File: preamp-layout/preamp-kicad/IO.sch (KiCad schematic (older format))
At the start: 14 parts, among them J36 Conn_Coaxial_x2, J37 Conn_Coaxial_x2, J38 Conn_Coaxial_x2, J39 Conn_Coaxial_x2, J40 Conn_Coaxial_x2, J41 Conn_01x03_Female, J42 Conn_01x03_Female, J43 Conn_01x03_Female, J44 Conn_01x03_Female, J45 Conn_01x03_Female, J46 Conn_01x03_Male, J47 Conn_01x03_Male, J48 Conn_Coaxial_x2, J49 Conn_Coaxial_x2

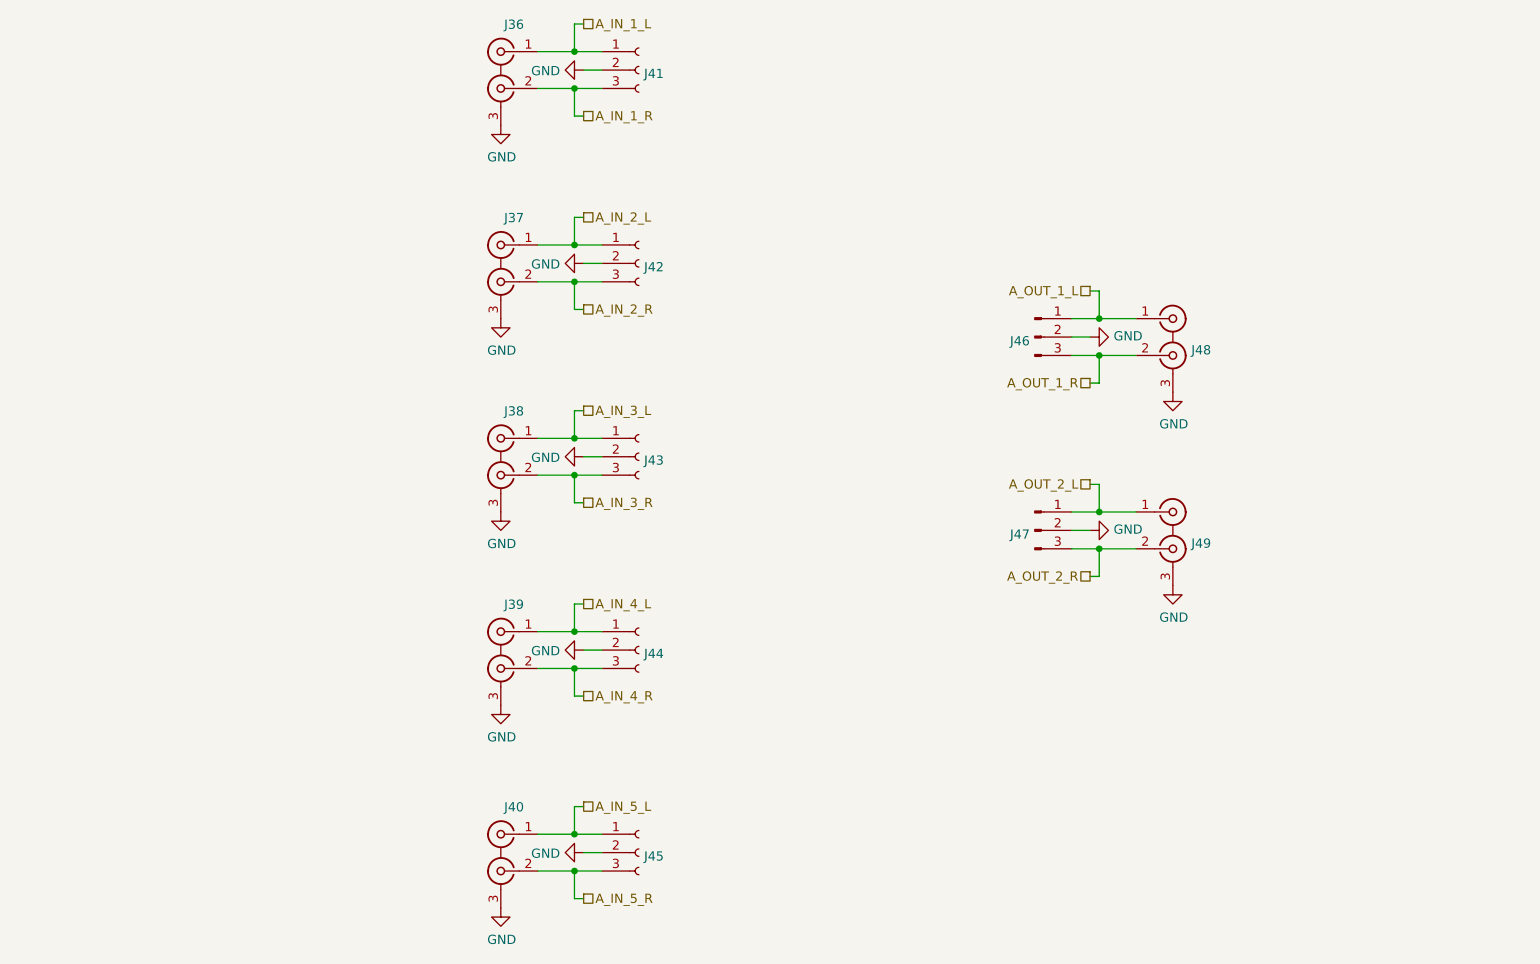
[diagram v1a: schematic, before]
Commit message: Power Supply Update
Grounding made more clear, tied to chassis on AC board. Pins renamed. Aligned with AC wall power convention. General cleanup.
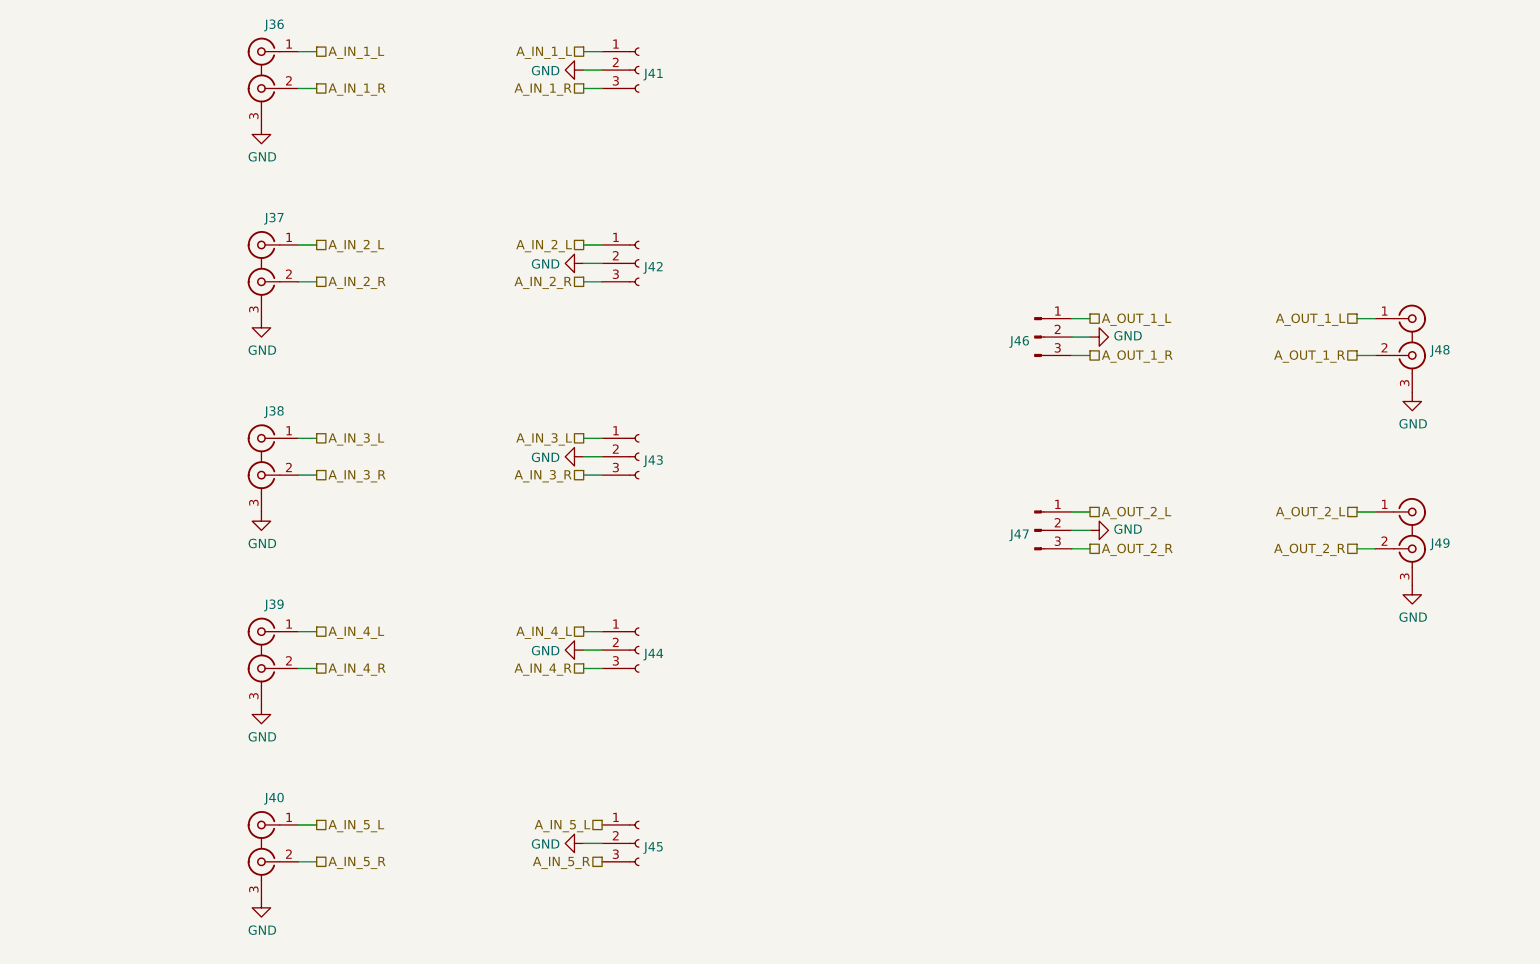
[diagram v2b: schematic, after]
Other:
- moved on the sheet: J36, J37, J38, J39, J40, J45, J48, J49

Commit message: Schematic layout updates
schematic optimization. Also implemented encoders with surrounding circuitry (self-contained on encoder board)
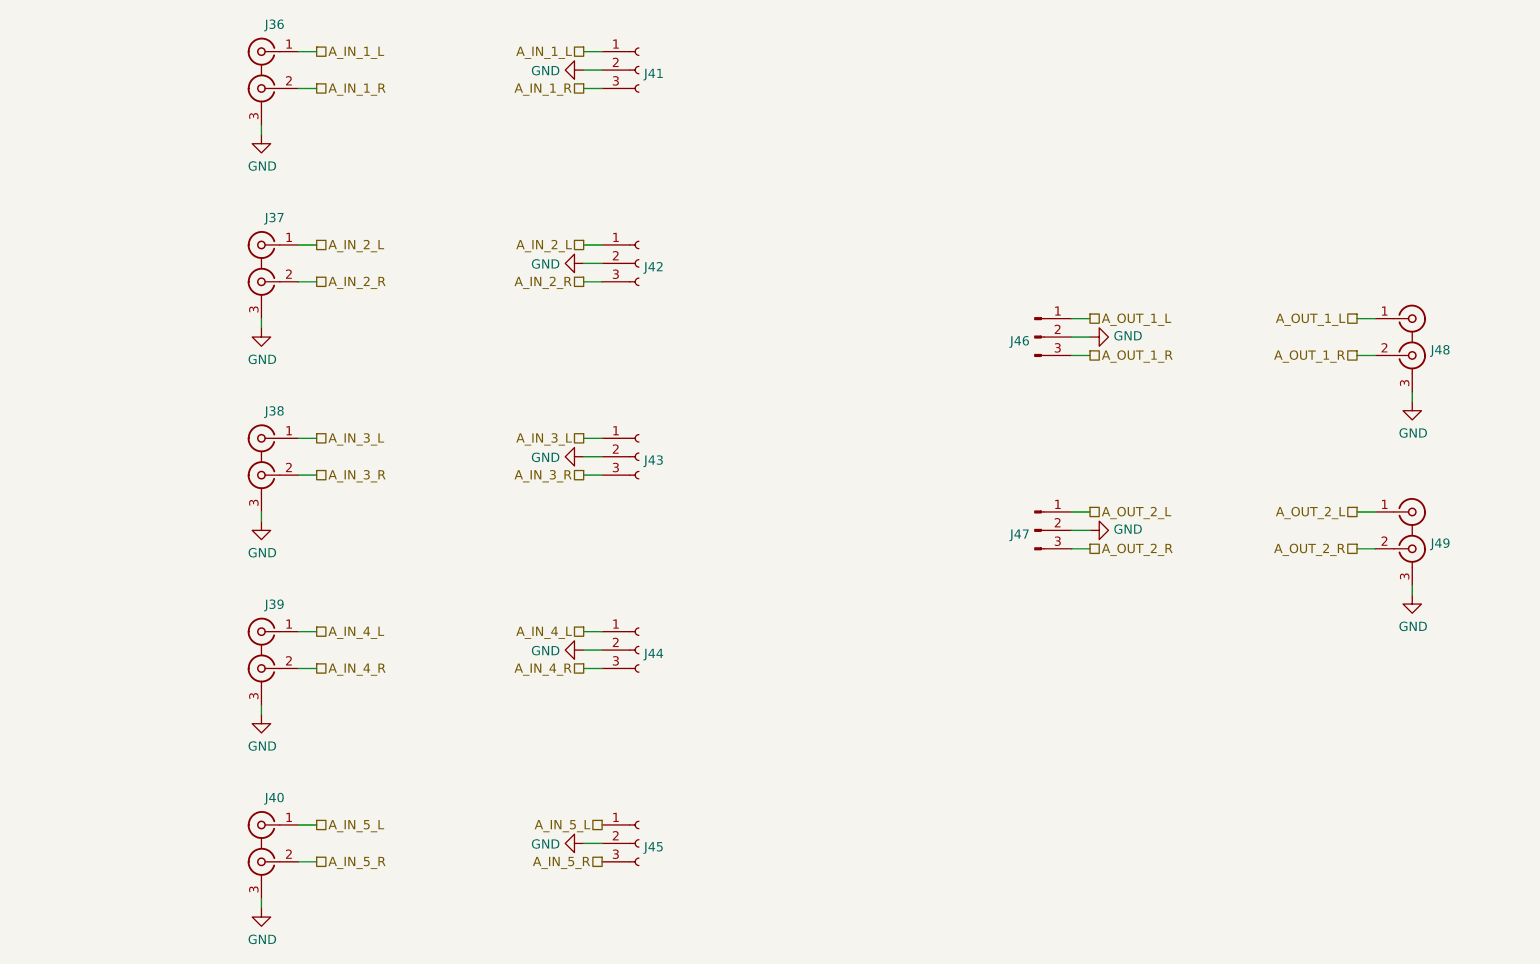
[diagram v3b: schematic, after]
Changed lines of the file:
@@
-$Comp
-L power:GND #PWR?
-U 1 1 64BAD508
-P 2800 6300
-AR Path="/5E26F6FE/64BAD508" Ref="#PWR?"  Part="1"
-AR Path="/5E607732/64BAD508" Ref="#PWR039"  Part="1"
-F 0 "#PWR039" H 2800 6050 50  0001 C CNN
-F 1 "GND" H 2805 6127 50  0000 C CNN
-F 2 "" H 2800 6300 50  0001 C CNN
-F 3 "" H 2800 6300 50  0001 C CNN
-	1    2800 6300
-	1    0    0    -1
-$EndComp
-$Comp
-L power:GND #PWR?
-U 1 1 64BAEC2E
-P 2800 5250
-AR Path="/5E26F6FE/64BAEC2E" Ref="#PWR?"  Part="1"
-AR Path="/5E607732/64BAEC2E" Ref="#PWR038"  Part="1"
-F 0 "#PWR038" H 2800 5000 50  0001 C CNN
-F 1 "GND" H 2805 5077 50  0000 C CNN
-F 2 "" H 2800 5250 50  0001 C CNN
-F 3 "" H 2800 5250 50  0001 C CNN
-	1    2800 5250
-	1    0    0    -1
-$EndComp
-$Comp
-L power:GND #PWR?
-U 1 1 64BB01CD
-P 2800 4200
-AR Path="/5E26F6FE/64BB01CD" Ref="#PWR?"  Part="1"
-AR Path="/5E607732/64BB01CD" Ref="#PWR037"  Part="1"
-F 0 "#PWR037" H 2800 3950 50  0001 C CNN
-F 1 "GND" H 2805 4027 50  0000 C CNN
-F 2 "" H 2800 4200 50  0001 C CNN
-F 3 "" H 2800 4200 50  0001 C CNN
-	1    2800 4200
-	1    0    0    -1
-$EndComp
-$Comp
-L power:GND #PWR?
-U 1 1 64BB1739
-P 2800 3150
-AR Path="/5E26F6FE/64BB1739" Ref="#PWR?"  Part="1"
-AR Path="/5E607732/64BB1739" Ref="#PWR036"  Part="1"
-F 0 "#PWR036" H 2800 2900 50  0001 C CNN
-F 1 "GND" H 2805 2977 50  0000 C CNN
-F 2 "" H 2800 3150 50  0001 C CNN
-F 3 "" H 2800 3150 50  0001 C CNN
-	1    2800 3150
-	1    0    0    -1
-$EndComp
 $Comp
 L power:GND #PWR?
 U 1 1 64BB2C61
-P 2800 2100
+P 2800 2150
 AR Path="/5E26F6FE/64BB2C61" Ref="#PWR?"  Part="1"
 AR Path="/5E607732/64BB2C61" Ref="#PWR035"  Part="1"
-F 0 "#PWR035" H 2800 1850 50  0001 C CNN
-F 1 "GND" H 2805 1927 50  0000 C CNN
-F 2 "" H 2800 2100 50  0001 C CNN
-F 3 "" H 2800 2100 50  0001 C CNN
-	1    2800 2100
-	1    0    0    -1
-$EndComp
-$Comp
-L power:GND #PWR?
-U 1 1 64BB4167
-P 9050 3550
-AR Path="/5E26F6FE/64BB4167" Ref="#PWR?"  Part="1"
-AR Path="/5E607732/64BB4167" Ref="#PWR047"  Part="1"
-F 0 "#PWR047" H 9050 3300 50  0001 C CNN
-F 1 "GND" H 9055 3377 50  0000 C CNN
-F 2 "" H 9050 3550 50  0001 C CNN
-F 3 "" H 9050 3550 50  0001 C CNN
-	1    9050 3550
-	1    0    0    -1
-$EndComp
-$Comp
-L power:GND #PWR?
-U 1 1 5EC97C75
-P 9050 4600
-AR Path="/5E26F6FE/5EC97C75" Ref="#PWR?"  Part="1"
-AR Path="/5E607732/5EC97C75" Ref="#PWR048"  Part="1"
-F 0 "#PWR048" H 9050 4350 50  0001 C CNN
-F 1 "GND" H 9055 4427 50  0000 C CNN
-F 2 "" H 9050 4600 50  0001 C CNN
-F 3 "" H 9050 4600 50  0001 C CNN
-	1    9050 4600
+F 0 "#PWR035" H 2800 1900 50  0001 C CNN
+F 1 "GND" H 2805 1977 50  0000 C CNN
+F 2 "" H 2800 2150 50  0001 C CNN
+F 3 "" H 2800 2150 50  0001 C CNN
+	1    2800 2150
 	1    0    0    -1
 $EndComp
@@
 Text HLabel 7300 4200 2    50   UnSpc ~ 0
 A_OUT_2_L
+Wire Wire Line
+	2800 2100 2800 2150
+$Comp
+L power:GND #PWR?
+U 1 1 5E790D2A
+P 9050 4650
+AR Path="/5E26F6FE/5E790D2A" Ref="#PWR?"  Part="1"
+AR Path="/5E607732/5E790D2A" Ref="#PWR0110"  Part="1"
+F 0 "#PWR0110" H 9050 4400 50  0001 C CNN
+F 1 "GND" H 9055 4477 50  0000 C CNN
+F 2 "" H 9050 4650 50  0001 C CNN
+F 3 "" H 9050 4650 50  0001 C CNN
+	1    9050 4650
+	1    0    0    -1
+$EndComp
+Wire Wire Line
+	9050 4600 9050 4650
+$Comp
+L power:GND #PWR?
+U 1 1 5E792160
+P 2800 3200
+AR Path="/5E26F6FE/5E792160" Ref="#PWR?"  Part="1"
+AR Path="/5E607732/5E792160" Ref="#PWR047"  Part="1"
+F 0 "#PWR047" H 2800 2950 50  0001 C CNN
+F 1 "GND" H 2805 3027 50  0000 C CNN
+F 2 "" H 2800 3200 50  0001 C CNN
+F 3 "" H 2800 3200 50  0001 C CNN
+	1    2800 3200
+	1    0    0    -1
+$EndComp
+Wire Wire Line
+	2800 3150 2800 3200
+$Comp
+L power:GND #PWR?
+U 1 1 5E792F4E
+P 2800 4250
+AR Path="/5E26F6FE/5E792F4E" Ref="#PWR?"  Part="1"
+AR Path="/5E607732/5E792F4E" Ref="#PWR048"  Part="1"
+F 0 "#PWR048" H 2800 4000 50  0001 C CNN
+F 1 "GND" H 2805 4077 50  0000 C CNN
+F 2 "" H 2800 4250 50  0001 C CNN
+F 3 "" H 2800 4250 50  0001 C CNN
+	1    2800 4250
+	1    0    0    -1
+$EndComp
+Wire Wire Line
+	2800 4200 2800 4250
+$Comp
+L power:GND #PWR?
+U 1 1 5E7942CF
+P 2800 5300
+AR Path="/5E26F6FE/5E7942CF" Ref="#PWR?"  Part="1"
+AR Path="/5E607732/5E7942CF" Ref="#PWR098"  Part="1"
+F 0 "#PWR098" H 2800 5050 50  0001 C CNN
+F 1 "GND" H 2805 5127 50  0000 C CNN
+F 2 "" H 2800 5300 50  0001 C CNN
+F 3 "" H 2800 5300 50  0001 C CNN
+	1    2800 5300
+	1    0    0    -1
+$EndComp
+Wire Wire Line
+	2800 5250 2800 5300
+$Comp
+L power:GND #PWR?
+U 1 1 5E795042
+P 2800 6350
+AR Path="/5E26F6FE/5E795042" Ref="#PWR?"  Part="1"
+AR Path="/5E607732/5E795042" Ref="#PWR0100"  Part="1"
+F 0 "#PWR0100" H 2800 6100 50  0001 C CNN
+F 1 "GND" H 2805 6177 50  0000 C CNN
+F 2 "" H 2800 6350 50  0001 C CNN
+F 3 "" H 2800 6350 50  0001 C CNN
+	1    2800 6350
+	1    0    0    -1
+$EndComp
+Wire Wire Line
+	2800 6300 2800 6350
+$Comp
+L power:GND #PWR?
+U 1 1 5E7983F2
+P 9050 3600
+AR Path="/5E26F6FE/5E7983F2" Ref="#PWR?"  Part="1"
+AR Path="/5E607732/5E7983F2" Ref="#PWR0109"  Part="1"
+F 0 "#PWR0109" H 9050 3350 50  0001 C CNN
+F 1 "GND" H 9055 3427 50  0000 C CNN
+F 2 "" H 9050 3600 50  0001 C CNN
+F 3 "" H 9050 3600 50  0001 C CNN
+	1    9050 3600
+	1    0    0    -1
+$EndComp
+Wire Wire Line
+	9050 3550 9050 3600
 $EndSCHEMATC
